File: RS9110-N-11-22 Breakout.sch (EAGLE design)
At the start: 13 parts, among them U1 RS9110-N-11-22

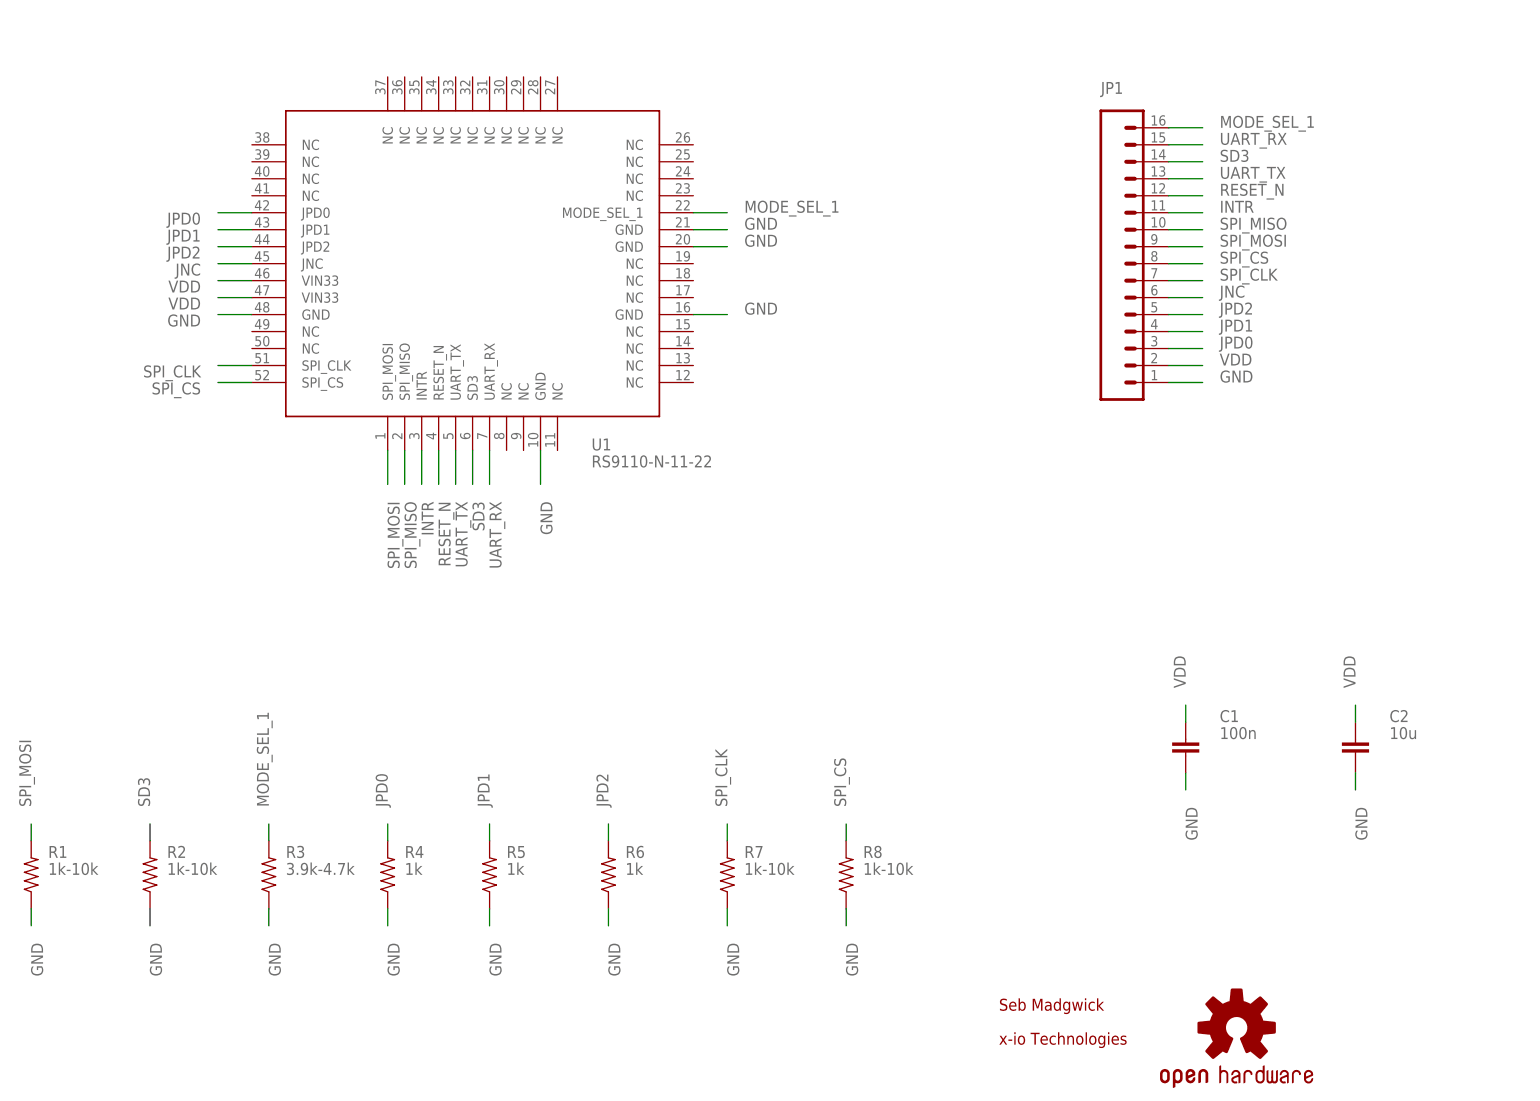
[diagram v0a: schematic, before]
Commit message: Add notes about when to populate resistors
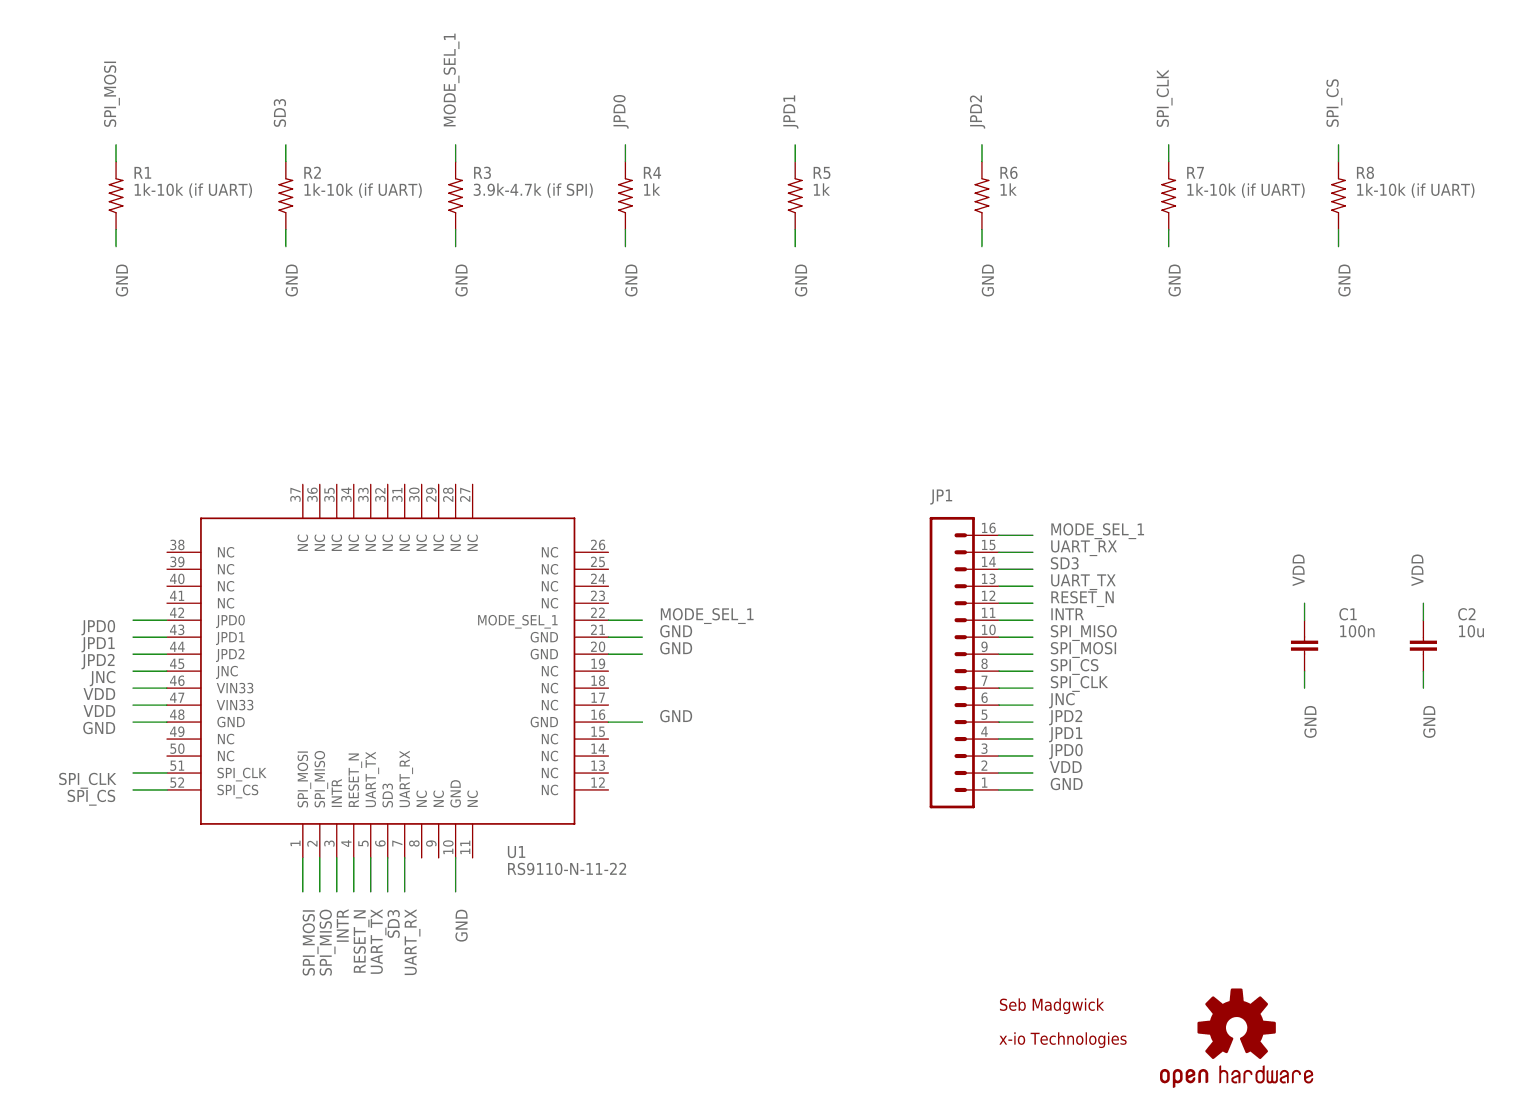
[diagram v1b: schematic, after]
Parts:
- R1, R2, R7, R8: value 1k-10k -> 1k-10k (if UART)
- R3: value 3.9k-4.7k -> 3.9k-4.7k (if SPI)
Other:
- moved on the sheet: C1, C2, JP1, R1, R2, R3, R4, R5, R6, R7, R8, U1
